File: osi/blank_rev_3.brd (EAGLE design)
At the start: 50.8 x 25.4 mm, 17 parts, among them IC1 MEGA8-AI, Y2 8Mhz

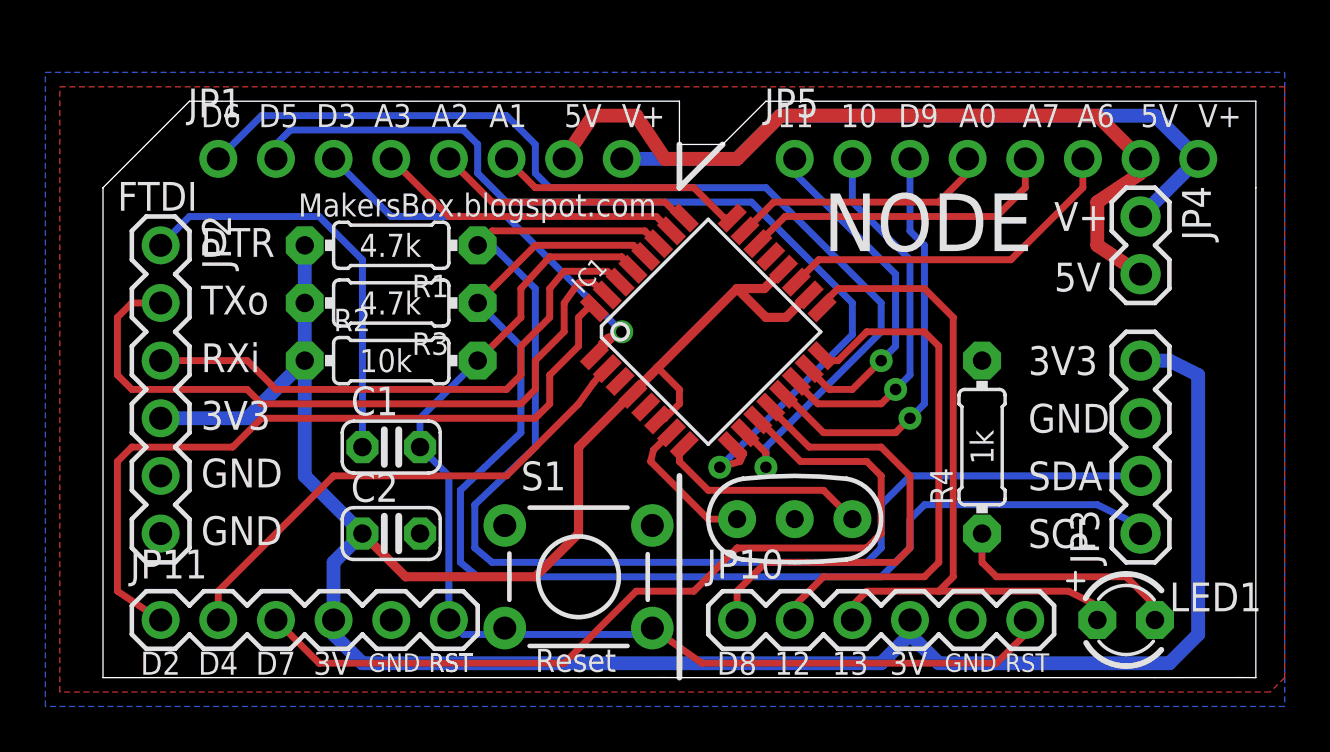
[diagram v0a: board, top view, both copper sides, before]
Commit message: moving headers
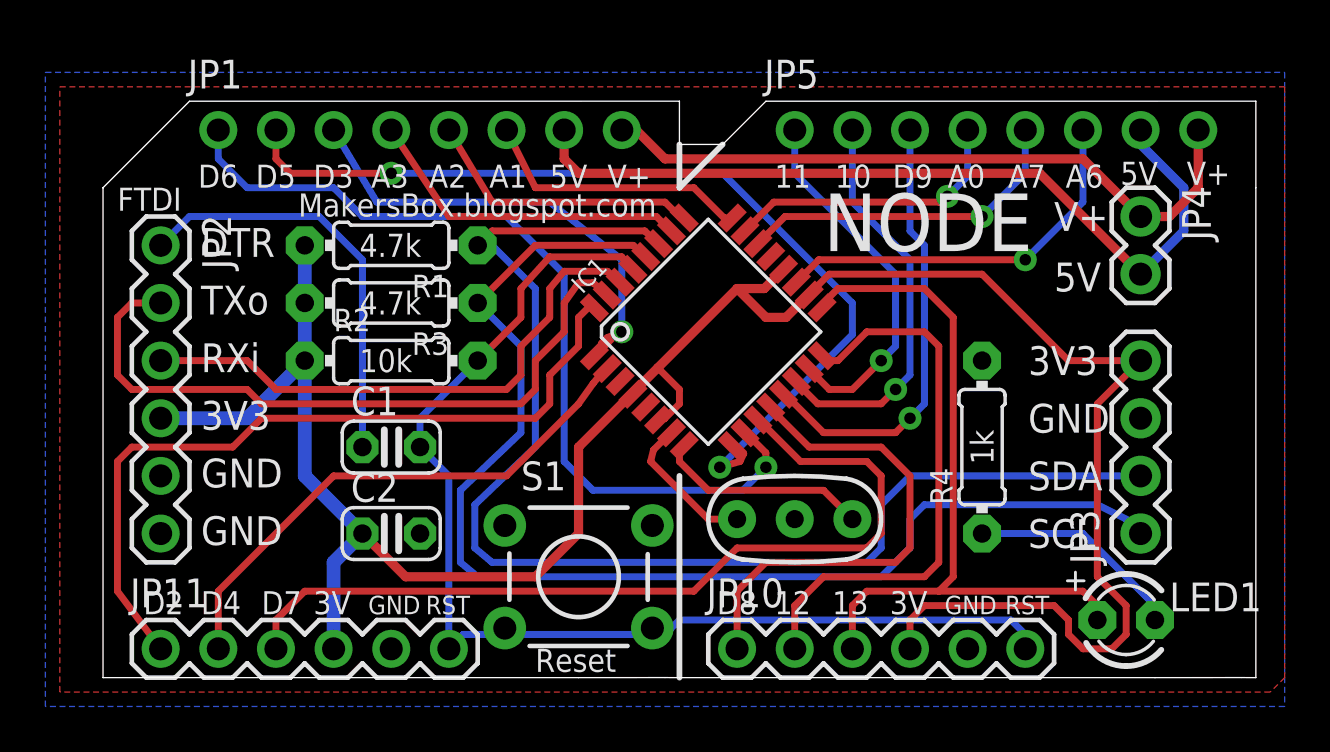
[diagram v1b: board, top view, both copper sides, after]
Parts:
- moved JP10 1.27 mm to (27.9, 1.27)
- moved JP11 1.27 mm to (2.54, 1.27)
- moved JP1 1.27 mm to (5.08, 24.1)
- moved JP5 1.27 mm to (30.5, 24.1)
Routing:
- net +3V3: track 115.6 -> 103.8 mm
- net D6: track 45.4 -> 38.7 mm
- net D3: track 19.7 -> 22.4 mm
- net A6: track 15.6 -> 17.3 mm, vias 0 -> 1
- net D13: track 31.6 -> 32.9 mm
- net A0: track 11.5 -> 12.8 mm, vias 0 -> 1
- net D8: track 20.3 -> 21.6 mm
- net D4: track 22.6 -> 23.9 mm
- net D12: track 23.4 -> 24.7 mm
- net D11: track 15.1 -> 16.4 mm
- net D10: track 16.6 -> 17.9 mm
- net D9: track 18.5 -> 19.8 mm
- net A1: track 11.0 -> 12.1 mm
- net A2: track 11.5 -> 12.5 mm
- net A3: track 13.7 -> 14.6 mm
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
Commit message: Leguino
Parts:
- added U$1: (no value), _my-parts:OREGON_09_52
- added U$2: (no value), _my-parts:OREGON_18_51
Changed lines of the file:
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@@
 <layer number="50" name="dxf" color="7" fill="1" visible="no" active="no"/>
 <layer number="51" name="tDocu" color="6" fill="1" visible="yes" active="yes"/>
-<layer number="52" name="bDocu" color="7" fill="1" visible="no" active="yes"/>
+<layer number="52" name="bDocu" color="7" fill="1" visible="yes" active="yes"/>
 <layer number="53" name="tGND_GNDA" color="7" fill="9" visible="no" active="no"/>
 <layer number="54" name="bGND_GNDA" color="1" fill="9" visible="no" active="no"/>
@@
 <element name="Y2" library="SparkFun_mod" package="RESONATOR-PTH" value="8Mhz" x="30.48" y="6.985"/>
 <element name="JP2" library="SparkFun_mod" package="1X06" value="" x="2.54" y="19.05" rot="R270"/>
+<element name="U$1" library="_my-parts" package="OREGON_09_52" value="" x="19.812" y="18.415"/>
+<element name="U$2" library="_my-parts" package="OREGON_18_51" value="" x="16.51" y="12.7"/>
 </elements>
 <signals>
